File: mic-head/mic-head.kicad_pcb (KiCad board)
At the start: 2 copper layers, 22 x 40 mm, 16 parts, among them J1 Loetpads_Kabel_5x, U1 TPS7A2028, U2 OPA2325

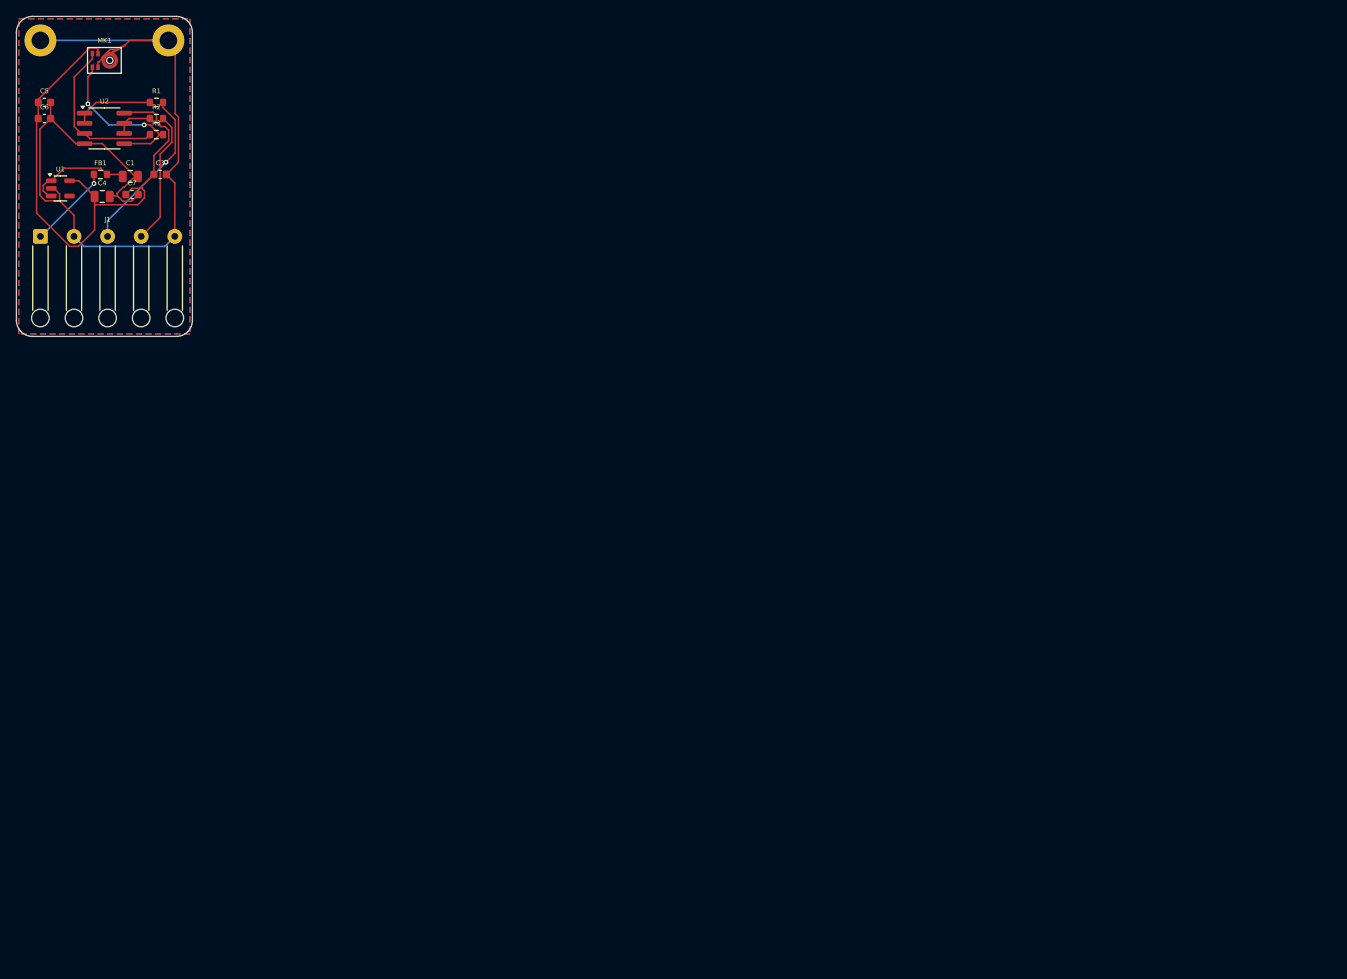
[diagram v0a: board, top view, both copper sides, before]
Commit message: modified:   01-power.kicad_sch 	modified:   02-analog.kicad_sch 	modified:   03-adc.kicad_sch 	modified:   04-mcu.kicad_sch 	modified:   05-io.kicad_sch 	new file:   exhaust-mic.kicad_pro 	modified:   exhaust-mic.kicad_sch 	modified:   mic-head/mic-head.kicad_pcb 	modified:   mic-head/mic-head.kicad_pro 	modified:   mic-head/mic-head.kicad_sch
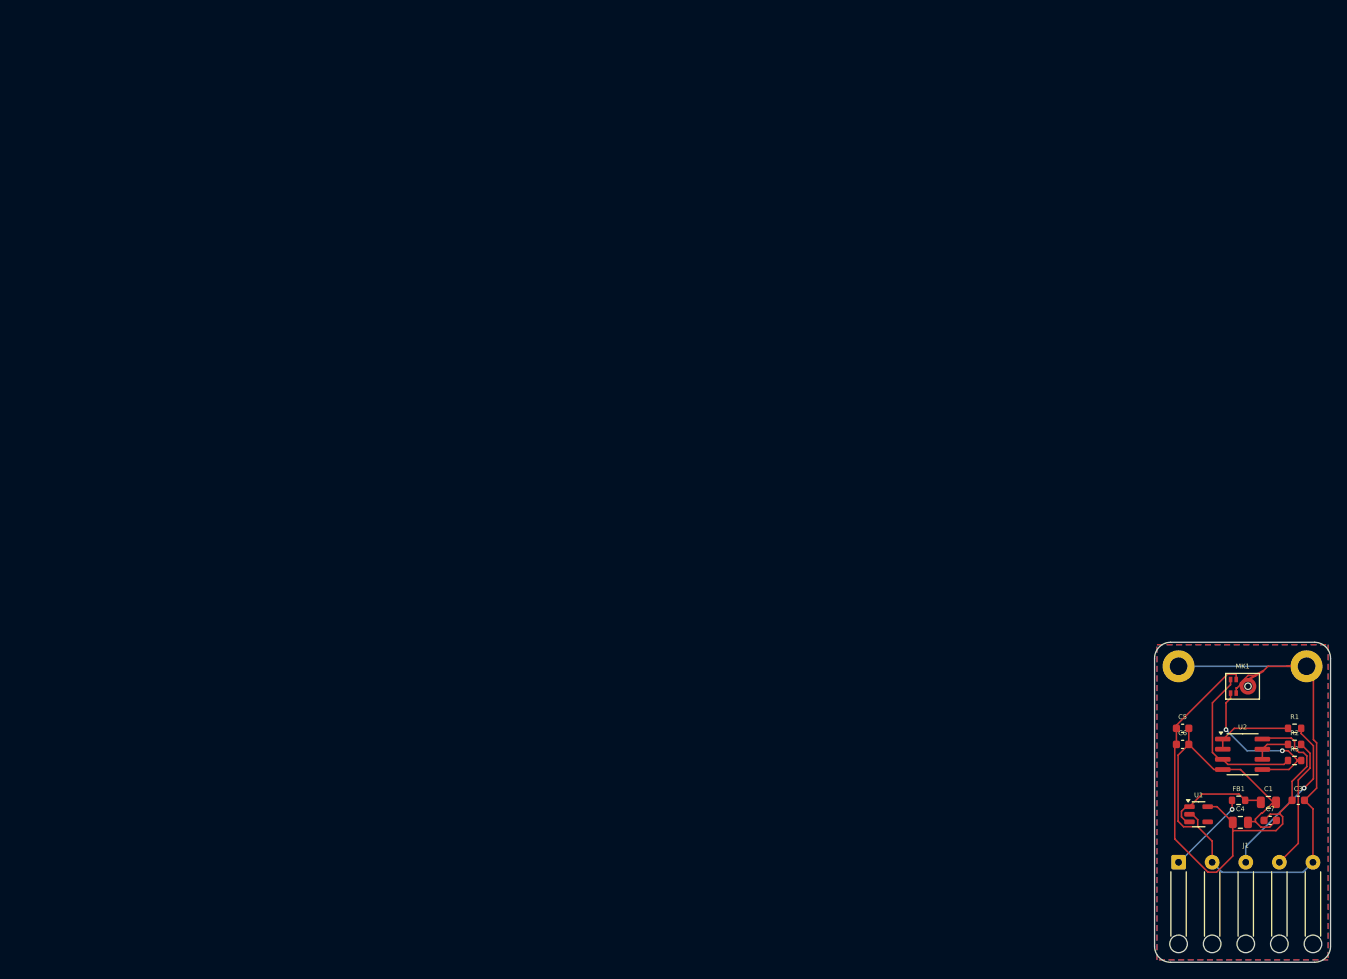
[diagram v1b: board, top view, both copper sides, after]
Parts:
- moved C3 162.4 mm to (160.2, 98.0)
- moved C4 162.4 mm to (153.0, 100.7)
- moved C5 162.4 mm to (145.8, 89.0)
- moved C6 162.4 mm to (145.8, 91.0)
- moved FB1 162.4 mm to (152.8, 98.0)
- moved H1 162.4 mm to (145.3, 81.2)
- moved H2 162.4 mm to (161.3, 81.2)
- moved J1 162.4 mm to (145.3, 105.7)
- moved MK1 162.4 mm to (153.3, 83.7)
- moved R1 162.4 mm to (159.8, 89.0)
- moved R2 162.4 mm to (159.8, 91.0)
- moved R3 162.4 mm to (159.8, 93.0)
- moved U1 162.4 mm to (147.8, 99.7)
- moved U2 162.4 mm to (153.3, 92.2)
- moved C1 162.4 mm to (156.5, 98.2)
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
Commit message: Layout verdrahten, ERC/DRC bereinigen, Werkzeugkette auf KiCad 10
Mikrofonkopf ist fertig verdrahtet (0 offene Verbindungen, 0 DRC-Fehler).
Auf der Hauptplatine bleiben 16 Verbindungen offen, ebenfalls ohne
DRC-Fehler; sie sind im interaktiven Router von KiCad zu schliessen.

Schaltplan
- 3 Speisepin-Fehler behoben (+4V6, ADC-AVDD, Uhrenbatterie brauchen ein
  Speiseflag - sie werden ueber Drossel, Ferrit bzw. Zelle gespeist und
  haben damit keine Quelle im Sinne der Regelpruefung)
- Netzname GND_CHASSIS entfernt: lag auf demselben Knoten wie GND
- TLV1117LV33 hatte einen Pin 4 fuer die Kuehlfahne, den es im Footprint
  SOT-223-3_TabPin2 nicht gibt - dort traegt Pad 2 die Fahne
- Piezo von Durchsteck- auf SMD-Ausfuehrung (Murata PKMCS0909E): fuer den
  12,5-mm-Typ gibt es keine Position, an der seine Anschluesse nicht auf
  der Gegenseite auf Pads treffen
- ERC laeuft jetzt fehlerfrei

Layout
- Durchsteckpads belegen beide Seiten. J1, J4 und J6 standen ueber
  rueckseitigen Bauteilen; das waren vier echte Kurzschluesse, unter
  anderem GPS_PPS gegen Masse an der Knopfzelle. Die eigene Pruefung
  vergleicht Durchsteckpads jetzt gegen beide Seiten, pad-genau
- In2 traegt keine Versorgungsinseln mehr, sondern Signale. Vorher wich
  der Autorouter auf die Masseflaeche aus - 140 Segmente aus 30 Netzen
  quer durch In1. Der DSN-Export kennzeichnet In1 nun als Versorgungslage
- Masseflaechen auf den Aussenlagen mit Naehvias an In1 angebunden und auf
  automatische Inselentfernung gestellt
- Netzklasse auf 0,18 mm Bahn, 0,15 mm Abstand, 0,5/0,25-mm-Via verengt;
  mit KiCads Vorgabewerten blieb rund ein Dutzend Verbindungen mehr offen
- Beschaffungsfelder unsichtbar und auf die Fab-Lage: sichtbar im
  Siebdruck ueberdecken die Herstellernummern die halbe Platine, das
  waren 151 der urspruenglich 214 Regelwarnungen

Werkzeuge
- pipeline.sh fasst den Layoutlauf zusammen
- fix_drc.py nimmt KiCads Regelpruefung als Instanz und entfernt, was sie
  beanstandet - die eigenen Abst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
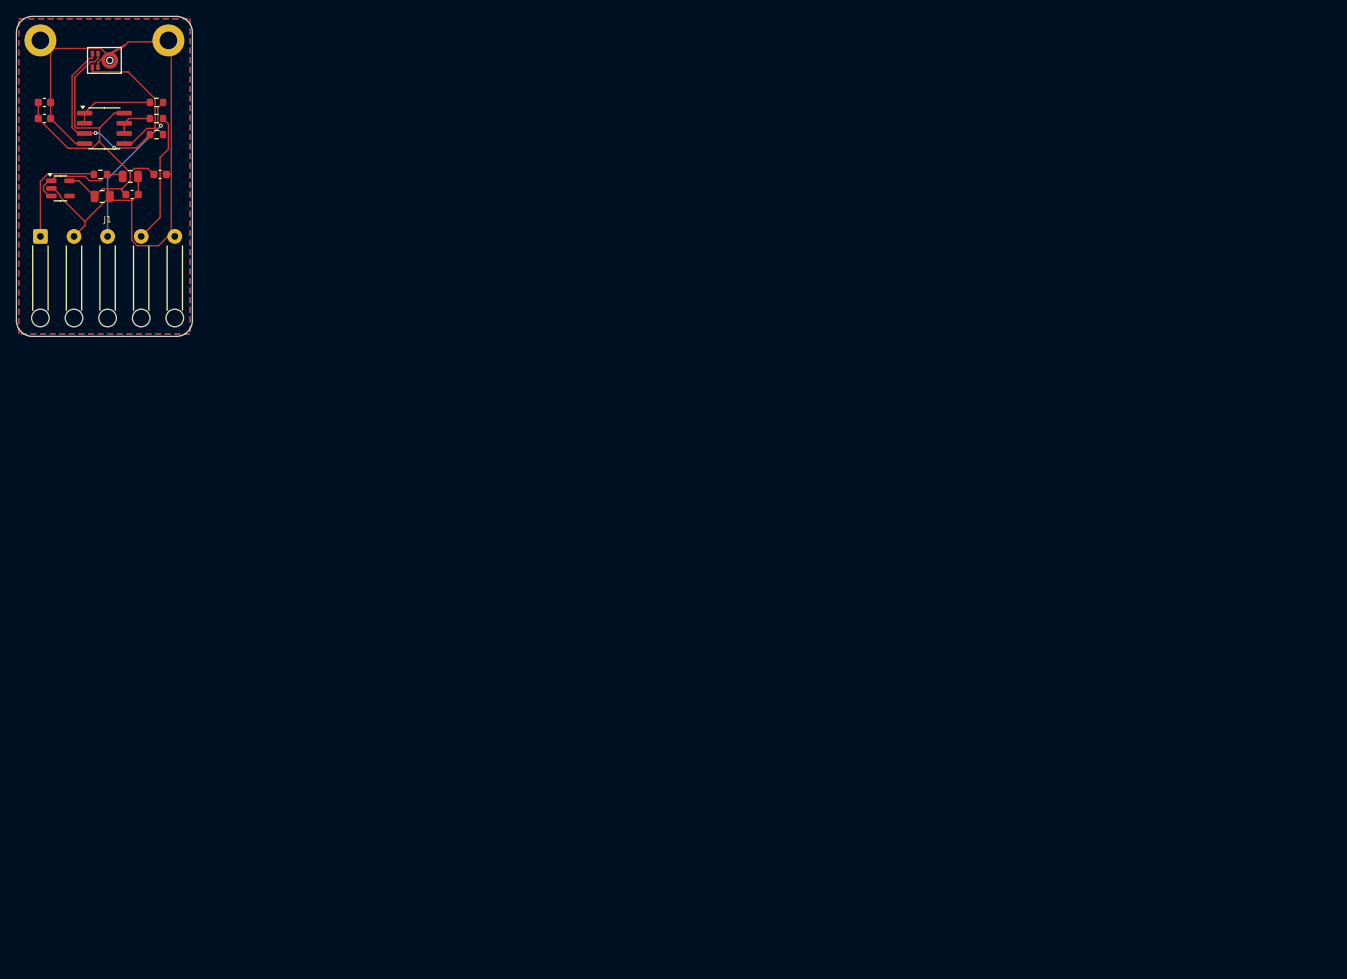
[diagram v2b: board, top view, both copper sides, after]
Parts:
- C1, C4: footprint C_0805_2012Metric -> Capacitor_SMD:C_0805_2012Metric
- C3, C5, C6, C7: footprint C_0603_1608Metric -> Capacitor_SMD:C_0603_1608Metric
- FB1, R1, R2, R3: footprint R_0603_1608Metric -> Resistor_SMD:R_0603_1608Metric
- J1: footprint SolderWire-0.25sqmm_1x05_P4.2mm_D0.65mm_OD1.7mm_Relief -> Connector_Wire:SolderWire-0.25sqmm_1x05_P4.2mm_D0.65mm_OD1.7mm_Relief
- MK1: footprint Infineon_PG-LLGA-5-1 -> exhaust-mic:Infineon_PG-LLGA-5-1
- U1: footprint SOT-23-5 -> Package_TO_SOT_SMD:SOT-23-5
- U2: footprint SOIC-8_3.9x4.9mm_P1.27mm -> Package_SO:SOIC-8_3.9x4.9mm_P1.27mm
- moved C3 162.4 mm to (18.0, 19.8)
- moved C4 162.4 mm to (10.7, 22.5)
- moved C5 162.4 mm to (3.50, 10.8)
- moved C6 162.4 mm to (3.50, 12.8)
- moved FB1 162.4 mm to (10.5, 19.8)
- moved H1 162.4 mm to (3.00, 3.00)
- moved H2 162.4 mm to (19.0, 3.00)
- moved J1 162.4 mm to (3.00, 27.5)
- moved MK1 162.4 mm to (11.0, 5.50)
- moved R1 162.4 mm to (17.5, 10.8)
- moved R2 162.4 mm to (17.5, 12.8)
- moved R3 162.4 mm to (17.5, 14.8)
- moved U1 162.4 mm to (5.50, 21.5)
- moved U2 162.4 mm to (11.0, 14.0)
- moved C1 162.4 mm to (14.2, 20.0)
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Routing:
- net SHIELD: track 113.1 -> 89.0 mm
- net +2V8: track 69.0 -> 50.9 mm
- net VIN_3V3: track 10.6 -> 14.0 mm, vias 1 -> 0
- net /MIC_P: track 20.3 -> 22.0 mm, vias 0 -> 2
- net /MIC_N: track 20.7 -> 19.5 mm, vias 2 -> 0
- net OUT_P: track 20.9 -> 19.9 mm

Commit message: modified:   01-power.kicad_sch 	modified:   02-analog.kicad_sch 	modified:   03-adc.kicad_sch 	modified:   04-mcu.kicad_sch 	modified:   05-io.kicad_sch 	modified:   exhaust-mic.kicad_pcb 	modified:   exhaust-mic.kicad_pro 	modified:   exhaust-mic.kicad_sch 	modified:   mic-head/mic-head.kicad_pcb 	modified:   mic-head/mic-head.kicad_pro 	modified:   mic-head/mic-head.kicad_sch 	new file:   ~exhaust-mic.kicad_pro.lck
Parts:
- moved C4 153.9 mm to (145.4, 97.0)
- moved C5 153.9 mm to (138.2, 85.3)
- moved C6 153.9 mm to (138.2, 87.3)
- moved R1 153.9 mm to (152.2, 85.3)
- moved R2 153.9 mm to (152.2, 87.3)
- moved R3 153.9 mm to (152.2, 89.3)
- moved C1 153.9 mm to (148.9, 94.5)
- moved C3 153.9 mm to (152.7, 94.3)
- moved C7 153.9 mm to (149.2, 96.8)
- moved FB1 153.9 mm to (145.2, 94.3)
- moved H1 153.9 mm to (137.7, 77.5)
- moved H2 153.9 mm to (153.7, 77.5)
- moved J1 153.9 mm to (137.7, 102.0)
- moved MK1 153.9 mm to (145.7, 80.0)
- moved U1 153.9 mm to (140.2, 96.0)
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
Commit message: J4 auf den GCT USB4085-GF-A umstellen und das Layout nachziehen
Den XKB-Typ zum bisherigen Footprint fuehrt DigiKey nicht. Der GCT
USB4085-GF-A ist lagernd (80 000 Stueck), kostet 0,78 EUR - aber es ist
keine gleiche Bauform: der XKB klebt mit einer Padreihe oben auf, der GCT
steckt mit sechzehn Anschluessen in zwei versetzten Reihen durch die
Platine. Am Motorrad ist das mechanisch die bessere Wahl; dafuer sperren
die Bohrungen alle vier Lagen.

tools/swap_footprint.py (neu) tauscht den Footprint auf der Platine und
ordnet die Netze ueber die Padnamen aus der Netzliste zu. Danach ist der
Autorouter einmal komplett durchgelaufen: 5 offene Verbindungen statt der
7 vorher, und keine davon auf einem Signalnetz - es sind nur noch
Masseflaechen-Stuecke auf der Rueckseite.

tools/trim_warnings.py (neu) raeumt lose Bahnenden und zu dicht gesetzte
Bohrungen weg, die KiCad nur als Warnung meldet. Einzeln, mit Rueckprobe:
pauschales Loeschen hat die Zahl der offenen Verbindungen von 5 auf 6
gehoben, weil ein als "lose" gemeldetes Stueck nach dem Fuellen der
Flaechen doch getragen hat. fix_drc.py kann jetzt ebenfalls Warnungen
mitnehmen (--alle), taugt dafuer aber nur mit Vorsicht.

Zwei echte Fehler in handroute.py behoben, die dabei auffielen:

* Bahnenden auf einer Innenlage wurden als "auf allen Lagen erreichbar"
  gelesen, weil das Muster nur F.Cu und B.Cu kannte. Ergebnis war eine
  Leiterbahn auf der Aussenlage zu einem Ende, das dort gar nicht liegt -
  Kupfer, das nichts verbindet, und ein Werkzeug, das Erfolg meldet.
* Der Anschlussdraht einer neu gesetzten Durchkontaktierung landete immer
  auf F.Cu oder B.Cu, egal wo das Bahnende lag.

Ausserdem darf handroute jetzt auf allen Signallagen ziehen, nicht nur auf
den beiden aeusseren; die durchgehende Masseflaeche auf In1 bleibt tabu.
route.py loest das Arbeitsverzeichnis absolut auf - mit relativer Angabe
fand Java das Jar nicht, weil freerouting mit dem Arbeitsverzeichnis als
cwd laeuft.

Zwei Bauteile sind im Lauf d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
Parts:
- U1: value TPS7A2028 -> LP5907MFX-2.8
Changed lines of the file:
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@@
 			)
 		)
-		(property "Value" "TPS7A2028"
+		(property "Value" "LP5907MFX-2.8"
 			(at 0 2.4 0)
 			(layer "F.Fab")
@@
 			)
 		)
-		(property "MPN" "TPS7A2028PDBVR"
+		(property "MPN" "LP5907MFX-2.8/NOPB"
 			(at 0 0 0)
 			(layer "F.Fab")
@@
 			)
 		)
-		(property "DigiKey" "296-TPS7A2028PDBVRCT-ND"
+		(property "DigiKey" "296-39063-1-ND"
 			(at 0 0 0)
 			(layer "F.Fab")
@@
 				)
 			)
+		)
+		(property "Hinweis" "Ersatz fuer TPS7A2028PDBVR: TPS7A2028 leer; LP5907 gleiche Belegung in SOT-23-5, 2,8 V, 6,5 uVrms - passt zur Mikrofonversorgung"
+			(at 0 0 0)
+			(layer "F.Fab")
+			(hide yes)
+			(effects
+				(font
+					(size 1.27 1.27)
+				)
+			)
